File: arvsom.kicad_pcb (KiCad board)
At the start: 12 copper layers, 55 x 40 mm, 456 parts, among them J1 TAG-10PIN, J3 DF40C-100DP-0.4V(51), J4 DF40C-100DP-0.4V(51), Q1 DMG1013UWQ-7, Q5 BSS138AKA, Q5 DMG1012UW, U1 MT53D1024M32D4DT-053, U10 TDA19988BHN_C1,557, U11 KSZ9031RNXCA, U13 VIC7100, U2 GD25LQ256DWIGR, U3 MT53D1024M32D4DT-053, U4 CSD86330Q3D, U5 LMR62014XMF_NOPB, U6 CSD86330Q3D, U7 STM811RW16F, U8 TPS65086100, Y1 ABM8G-25.000MHZ-18-D2Y-T, Y2 ABM8G-25.000MHZ-18-D2Y-T, Y3 ABM8G-27.000MHZ-18-D2Y-T

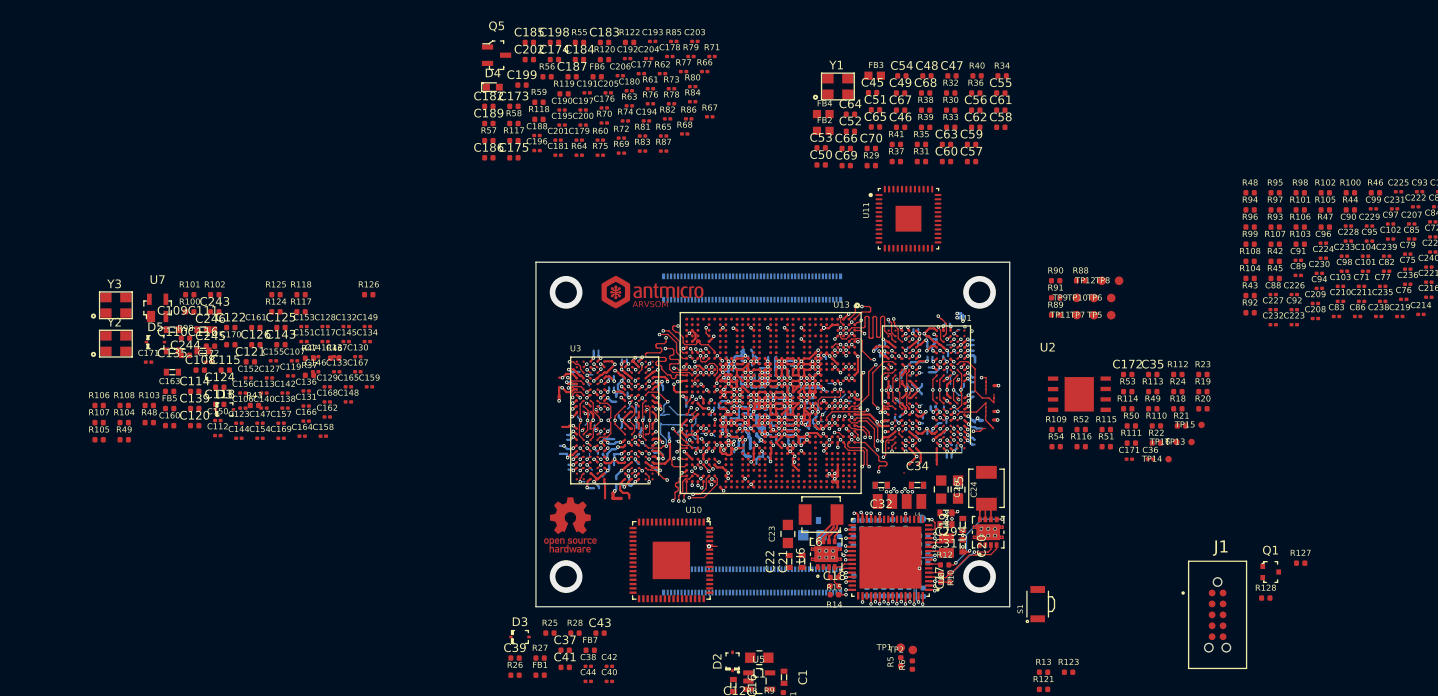
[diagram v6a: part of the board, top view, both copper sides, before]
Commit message: Replaced 33R groups with resistor arrays
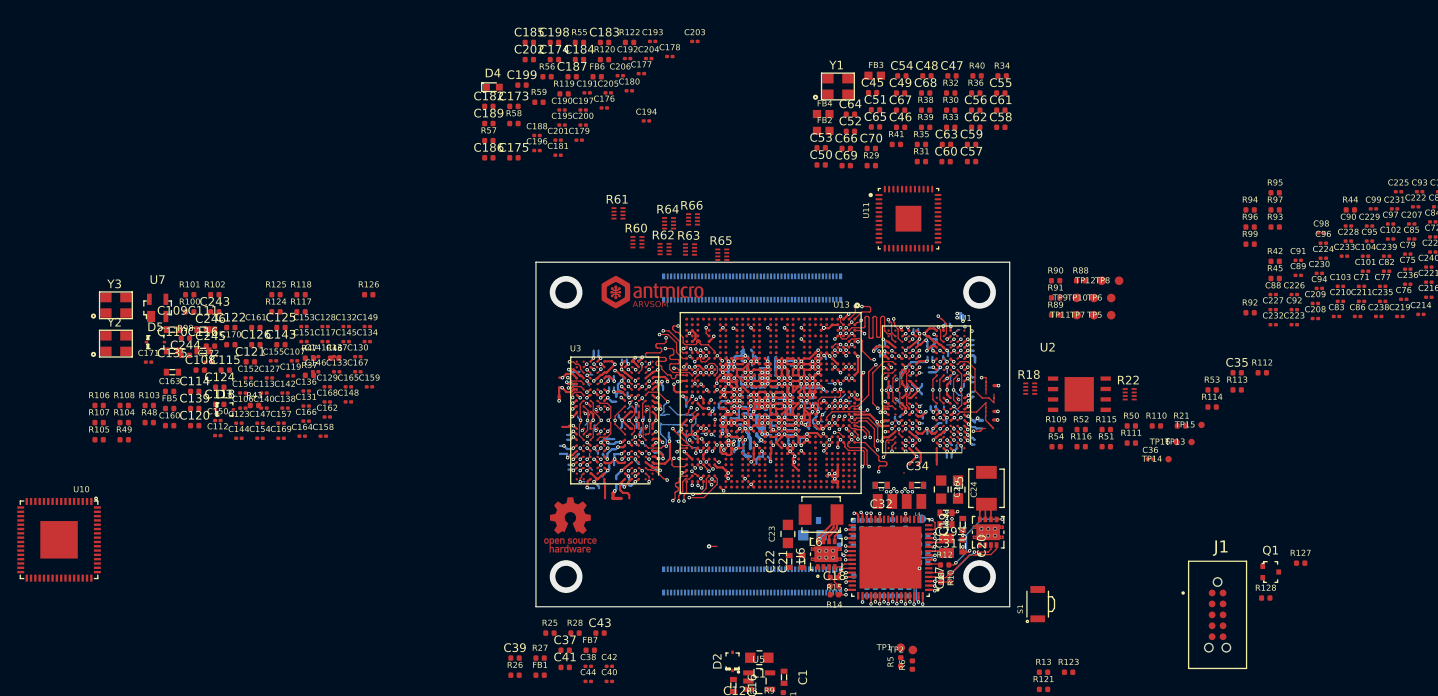
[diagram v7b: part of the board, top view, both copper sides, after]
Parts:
- removed the C171 at (198.9, 77.8)
- removed the C172 at (198.7, 68.0)
- removed the D3 at (128.2, 98.5)
- removed the Q5 at (125.4, 30.9)
- removed the R100 at (224.6, 46.9)
- removed the R101 at (218.8, 48.9)
- removed the R102 at (221.7, 46.9)
- removed the R103 at (218.8, 52.9)
- removed the R104 at (212.9, 56.9)
- removed the R105 at (221.7, 48.9)
- removed the R106 at (218.8, 50.9)
- removed the R107 at (215.8, 52.9)
- removed the R108 at (212.9, 54.9)
- removed the R117 at (127.5, 40.9)
- removed the R118 at (130.4, 38.4)
- removed the R121 at (173.0, 88.1)
- removed the R13 at (175.0, 93.3)
- removed R19, R20, R23, R24: R_33R_0402, arvsom-footprints:0402-res
- removed the R37 at (171.9, 43.3)
- removed the R43 at (212.9, 58.9)
- removed the R46 at (227.5, 46.9)
- removed the R47 at (221.7, 50.9)
- removed the R48 at (212.9, 46.9)
- removed the R49 at (201.6, 72.0)
- removed R67, R68, R69, R70, R71, R72, R73, R74, R75, R76, R77, R78, R79, R80, R81, R82, R83, R84, R85, R86, R87: R_33R_0201, arvsom-footprints:0201-res
- removed the R98 at (218.8, 46.9)
- R18, R22: value R_33R_0402 -> 4x33R_0201_array; footprint arvsom-footprints:0402-res -> arvsom-footprints:EXB18V
- R60, R61, R62, R63, R64, R65, R66: value R_33R_0201 -> 4x33R_0201_array; footprint arvsom-footprints:0201-res -> arvsom-footprints:EXB18V
- moved U10 71.1 mm to (74.7, 87.2)
- moved R62 20.4 mm to (144.9, 53.5)
- moved R63 18.1 mm to (147.9, 53.5)
- moved R18 17.3 mm to (187.4, 69.7)
- moved R66 17.2 mm to (148.2, 50.0)
- moved R65 15.4 mm to (151.7, 54.1)
- moved R61 14.9 mm to (139.6, 49.3)
- moved R64 13.1 mm to (145.5, 50.5)
- moved R60 12.6 mm to (141.8, 52.6)
- moved C35 9.80 mm to (211.4, 67.8)
- moved R112 9.80 mm to (214.3, 67.8)
- moved R113 9.80 mm to (211.4, 69.8)
- moved R114 9.80 mm to (208.5, 71.8)
- moved R53 9.80 mm to (208.5, 69.8)
- moved R22 6.46 mm to (198.9, 70.3)
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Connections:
- R18 pad 2: Net-(R18-Pad2) -> QSPI_D1
- R21 pad 2: Net-(R18-Pad2) -> Net-(R18-Pad8)
- R22 pad 2: QSPI_D3 -> Net-(R22-Pad2)
- R60 pad 2: Net-(R60-Pad2) -> LCD_DE
- R61 pad 1: LCD_DE -> LCD_DATA0
- R61 pad 2: Net-(R61-Pad2) -> LCD_DATA1
- R62 pad 1: LCD_VSYNC -> LCD_DATA4
- R62 pad 2: Net-(R62-Pad2) -> LCD_DATA5
- R63 pad 1: LCD_HSYNC -> LCD_DATA8
- R63 pad 2: Net-(R63-Pad2) -> LCD_DATA9
- R64 pad 1: LCD_DATA0 -> LCD_DATA12
- R64 pad 2: Net-(R64-Pad2) -> LCD_DATA13
- R65 pad 1: LCD_DATA1 -> LCD_DATA16
- R65 pad 2: Net-(R65-Pad2) -> LCD_DATA17
- R66 pad 1: LCD_DATA2 -> LCD_DATA20
- R66 pad 2: Net-(R66-Pad2) -> LCD_DATA21
- U13 pad AA1: Net-(R62-Pad2) -> Net-(R60-Pad6)
- U13 pad AA2: Net-(R67-Pad2) -> Net-(R61-Pad5)
- U13 pad AA3: Net-(R60-Pad2) -> Net-(R60-Pad8)
- U13 pad AA4: Net-(R61-Pad2) -> Net-(R60-Pad7)
- U13 pad AA5: Net-(R64-Pad2) -> Net-(R61-Pad8)
- U13 pad AA6: Net-(R65-Pad2) -> Net-(R61-Pad7)
- U13 pad AB1: Net-(R66-Pad2) -> Net-(R61-Pad6)
- U13 pad AB2: Net-(R71-Pad2) -> Net-(R62-Pad5)
- U13 pad AB4: Net-(R75-Pad2) -> Net-(R63-Pad5)
- U13 pad AB5: Net-(R68-Pad2) -> Net-(R62-Pad8)
- U13 pad AB6: Net-(R69-Pad2) -> Net-(R62-Pad7)
- U13 pad AB7: Net-(R72-Pad2) -> Net-(R63-Pad8)
- U13 pad AC1: Net-(R70-Pad2) -> Net-(R62-Pad6)
- U13 pad AD1: Net-(R74-Pad2) -> Net-(R63-Pad6)
- U13 pad AD2: Net-(R79-Pad2) -> Net-(R64-Pad5)
- U13 pad AD3: Net-(R82-Pad2) -> Net-(R65-Pad6)
- U13 pad AD4: Net-(R86-Pad2) -> Net-(R66-Pad6)
- U13 pad AD5: Net-(R87-Pad2) -> Net-(R66-Pad5)
- U13 pad AE1: Net-(R78-Pad2) -> Net-(R64-Pad6)
- U13 pad AE2: Net-(R83-Pad2) -> Net-(R65-Pad5)
- U13 pad AE4: Net-(R84-Pad2) -> Net-(R66-Pad8)
- U13 pad AG2: Net-(R73-Pad2) -> Net-(R63-Pad7)
- U13 pad AG3: Net-(R77-Pad2) -> Net-(R64-Pad7)
- U13 pad AG4: Net-(R81-Pad2) -> Net-(R65-Pad7)
- U13 pad AL3: Net-(R80-Pad2) -> Net-(R65-Pad8)
- U13 pad Y2: Net-(R63-Pad2) -> Net-(R60-Pad5)
- U2 pad 1: Net-(R18-Pad2) -> Net-(R18-Pad8)
- U2 pad 2: Net-(R19-Pad2) -> Net-(R18-Pad7)
- U2 pad 3: Net-(R20-Pad2) -> Net-(R18-Pad6)
- U2 pad 6: Net-(R23-Pad1) -> Net-(R22-Pad2)
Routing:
- net Net-(R81-Pad2): track 1.75 -> 0.00 mm, vias 1 -> 0
- net Net-(R65-Pad7): track 0.00 -> 1.75 mm, vias 0 -> 1
